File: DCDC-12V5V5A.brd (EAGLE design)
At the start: 40 x 23 mm, 34 parts, among them CN2 2828XX-2282834-2, CN3 2828XX-2282834-2, Q10 NMOSFET, Q9 NMOSFET, U1 LM3150MHX/NOPB

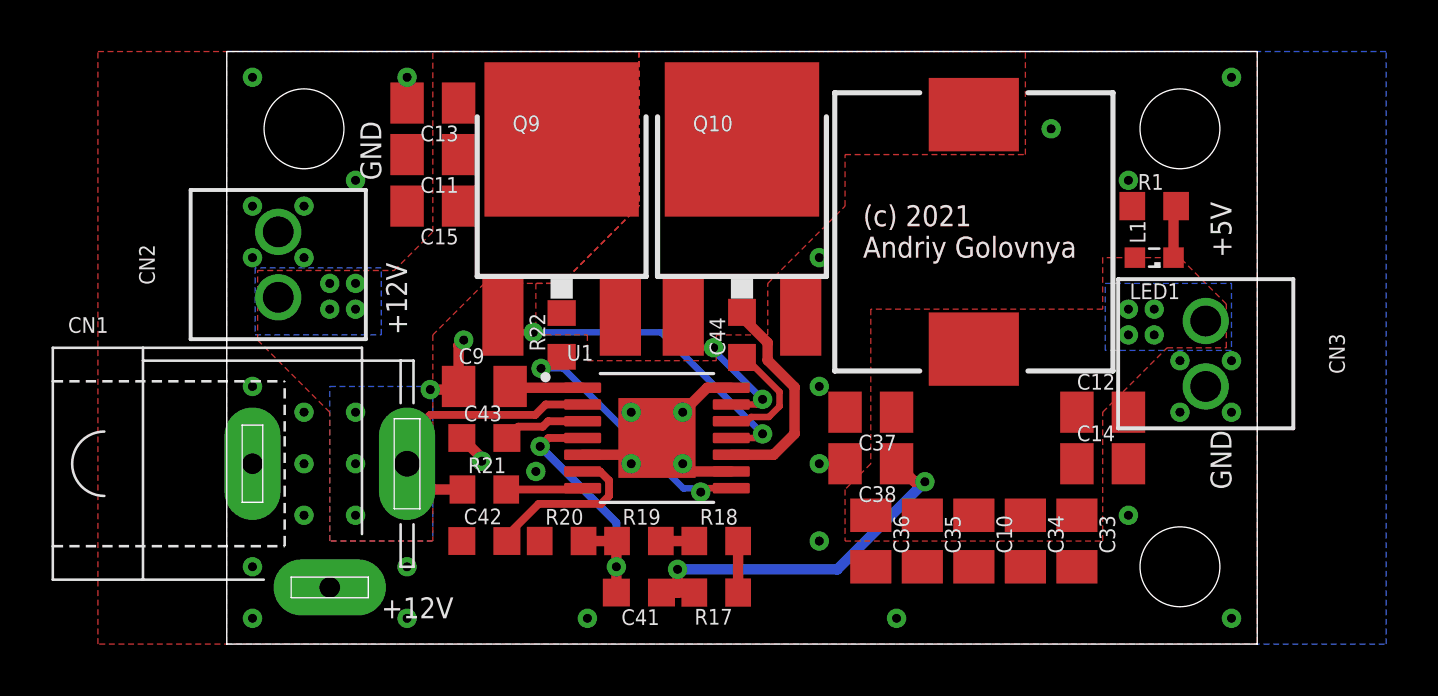
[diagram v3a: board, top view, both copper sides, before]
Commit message: Minor improvements in board routing. Generated CAM files. Fixed footprints in BoM.
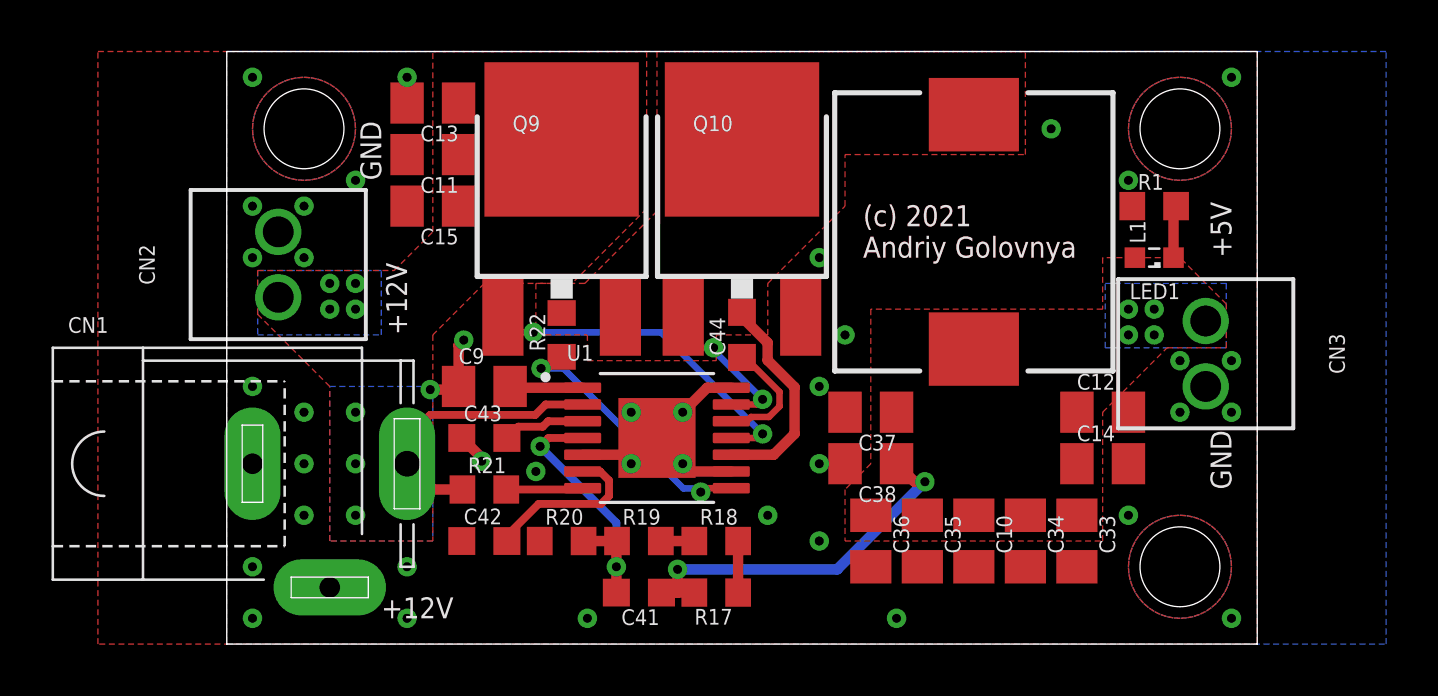
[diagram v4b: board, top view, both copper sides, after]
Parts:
- moved LOGO2 1.00 mm to (23.0, 1.00)
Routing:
- net GND: vias 38 -> 40
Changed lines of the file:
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@@
 <text x="4.1" y="14.5" size="0.8128" layer="22" font="vector" rot="MR270">+12V</text>
 <text x="4.1" y="17.1" size="0.8128" layer="22" font="vector" rot="MR270">GND</text>
-<text x="36.7" y="10.9" size="0.8128" layer="22" font="vector" rot="MR270">+5V</text>
-<text x="36.7" y="13.7" size="0.8128" layer="22" font="vector" rot="MR270">GND</text>
+<text x="36.7" y="13.5" size="0.8128" layer="22" font="vector" rot="MR270">+5V</text>
+<text x="36.7" y="11" size="0.8128" layer="22" font="vector" rot="MR270">GND</text>
 <text x="33" y="13" size="0.8128" layer="22" font="vector" rot="MR0">http://redscorp.net</text>
 <text x="24.7" y="15" size="0.8128" layer="1" font="vector" ratio="12">(c) 2021
@@
 </element>
 <element name="LOGO1" library="_my_logos" package="RSNURL_QR_8MM" value="RSNURL_QR_8MM" x="33" y="3" smashed="yes" rot="MR0"/>
-<element name="LOGO2" library="_my_logos" package="MFDEC_L_10MM" value="MFDECLOGO_L_10MM" x="24" y="1" smashed="yes" rot="MR0"/>
+<element name="LOGO2" library="_my_logos" package="MFDEC_L_10MM" value="MFDECLOGO_L_10MM" x="23" y="1" smashed="yes" rot="MR0"/>
 <element name="LED1" library="led" library_urn="urn:adsk.eagle:library:259" package="SML0603" package3d_urn="urn:adsk.eagle:package:15832/1" value="GREEN" x="36" y="15" smashed="yes" rot="R180">
 <attribute name="NAME" x="37" y="14" size="0.6096" layer="25" font="vector" rot="R180"/>
@@
 <vertex x="8" y="16"/>
 <vertex x="8" y="23"/>
-<vertex x="16" y="23"/>
-<vertex x="16" y="17"/>
-<vertex x="13" y="14"/>
+<vertex x="16.3" y="23"/>
+<vertex x="16.3" y="16.9"/>
+<vertex x="13.4" y="14"/>
 <vertex x="10" y="14"/>
 <vertex x="8" y="12"/>
 <vertex x="8" y="4"/>
 <vertex x="4" y="4"/>
-<vertex x="4" y="9"/>
-<vertex x="1.2" y="11.8"/>
-</polygon>
-<polygon width="0.1524" layer="16" thermals="no">
-<vertex x="1.1" y="14.6"/>
-<vertex x="1.1" y="12"/>
+<vertex x="4" y="10"/>
+<vertex x="1.2" y="12.8"/>
+</polygon>
+<polygon width="0.254" layer="16" thermals="no">
+<vertex x="1.2" y="14.5"/>
+<vertex x="1.2" y="12"/>
 <vertex x="6" y="12"/>
-<vertex x="6" y="14.6"/>
-</polygon>
-<polygon width="0.1524" layer="16" thermals="no">
+<vertex x="6" y="14.5"/>
+</polygon>
+<polygon width="0.254" layer="16" thermals="no">
 <vertex x="8" y="4"/>
 <vertex x="4" y="4"/>
@@
 <via x="1" y="10" extent="1-16" drill="0.35"/>
 <contactref element="R1" pad="1"/>
+<via x="24" y="12" extent="1-16" drill="0.35"/>
+<via x="21" y="5" extent="1-16" drill="0.35"/>
+<polygon width="0.1524" layer="1" pour="cutout">
+<vertex x="37" y="1" curve="-180"/>
+<vertex x="37" y="5" curve="-180"/>
+</polygon>
+<polygon width="0.1524" layer="1" pour="cutout">
+<vertex x="37" y="18" curve="-180"/>
+<vertex x="37" y="22" curve="-180"/>
+</polygon>
+<polygon width="0.1524" layer="1" pour="cutout">
+<vertex x="3" y="18" curve="-180"/>
+<vertex x="3" y="22" curve="-180"/>
+</polygon>
+<polygon width="0.1524" layer="16" pour="cutout">
+<vertex x="3" y="18" curve="-180"/>
+<vertex x="3" y="22" curve="-180"/>
+</polygon>
+<polygon width="0.1524" layer="16" pour="cutout">
+<vertex x="37" y="18" curve="-180"/>
+<vertex x="37" y="22" curve="-180"/>
+</polygon>
+<polygon width="0.1524" layer="16" pour="cutout">
+<vertex x="37" y="1" curve="-180"/>
+<vertex x="37" y="5" curve="-180"/>
+</polygon>
 </signal>
 <signal name="5V">
@@
 <vertex x="34" y="13"/>
 </polygon>
-<polygon width="0.1524" layer="16" thermals="no">
-<vertex x="39" y="11.4"/>
-<vertex x="34.1" y="11.4"/>
+<polygon width="0.254" layer="16" thermals="no">
+<vertex x="38.8" y="11.5"/>
+<vertex x="34.1" y="11.5"/>
 <vertex x="34.1" y="14"/>
-<vertex x="39" y="14"/>
+<vertex x="38.8" y="14"/>
 </polygon>
 <via x="35" y="13" extent="1-16" drill="0.35"/>
@@
 <vertex x="31" y="19"/>
 <vertex x="31" y="23"/>
-<vertex x="16" y="23"/>
-<vertex x="16" y="17"/>
-<vertex x="13" y="14"/>
+<vertex x="16.7" y="23"/>
+<vertex x="16.7" y="16.8"/>
+<vertex x="13.9" y="14"/>
 <vertex x="12" y="14"/>
 <vertex x="12" y="12"/>

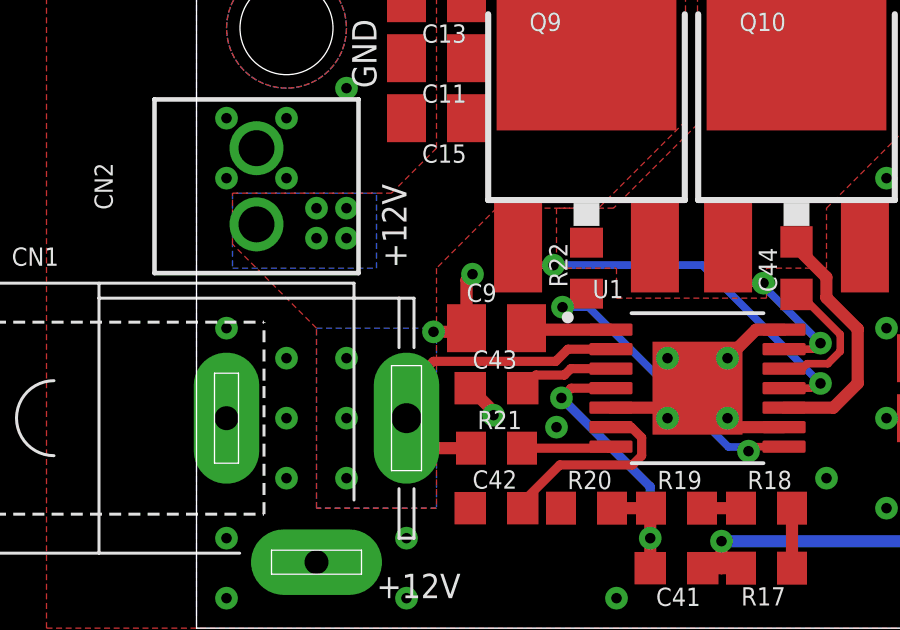
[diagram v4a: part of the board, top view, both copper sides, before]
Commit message: Minor improvements in board routing. Generated CAM files.
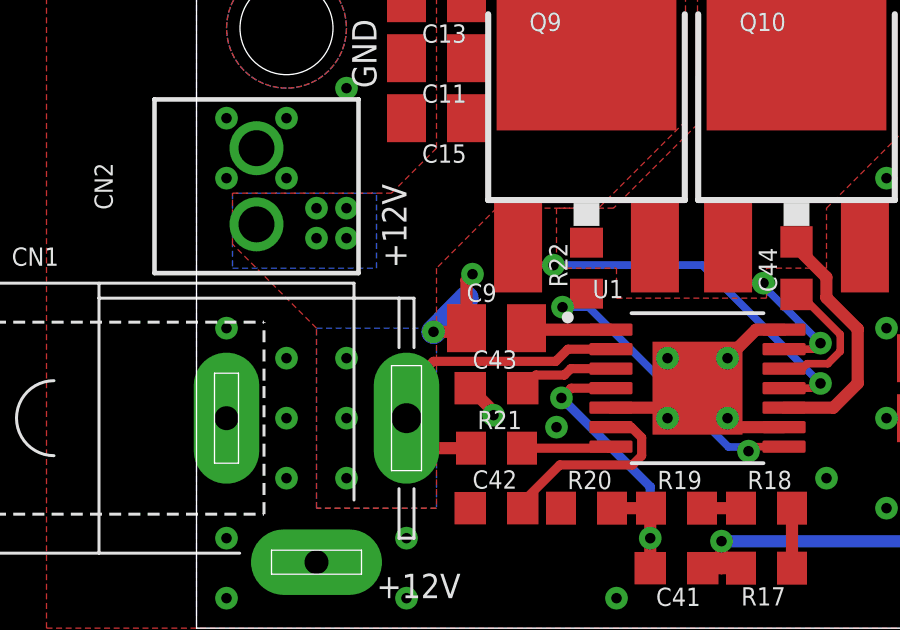
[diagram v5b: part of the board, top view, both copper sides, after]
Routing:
- net GND: track 10.6 -> 12.1 mm
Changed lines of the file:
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@@
 <vertex x="37" y="5" curve="-180"/>
 </polygon>
+<wire x1="7.9" y1="9.8782" x2="9" y2="11" width="0.8128" layer="16"/>
 </signal>
 <signal name="5V">

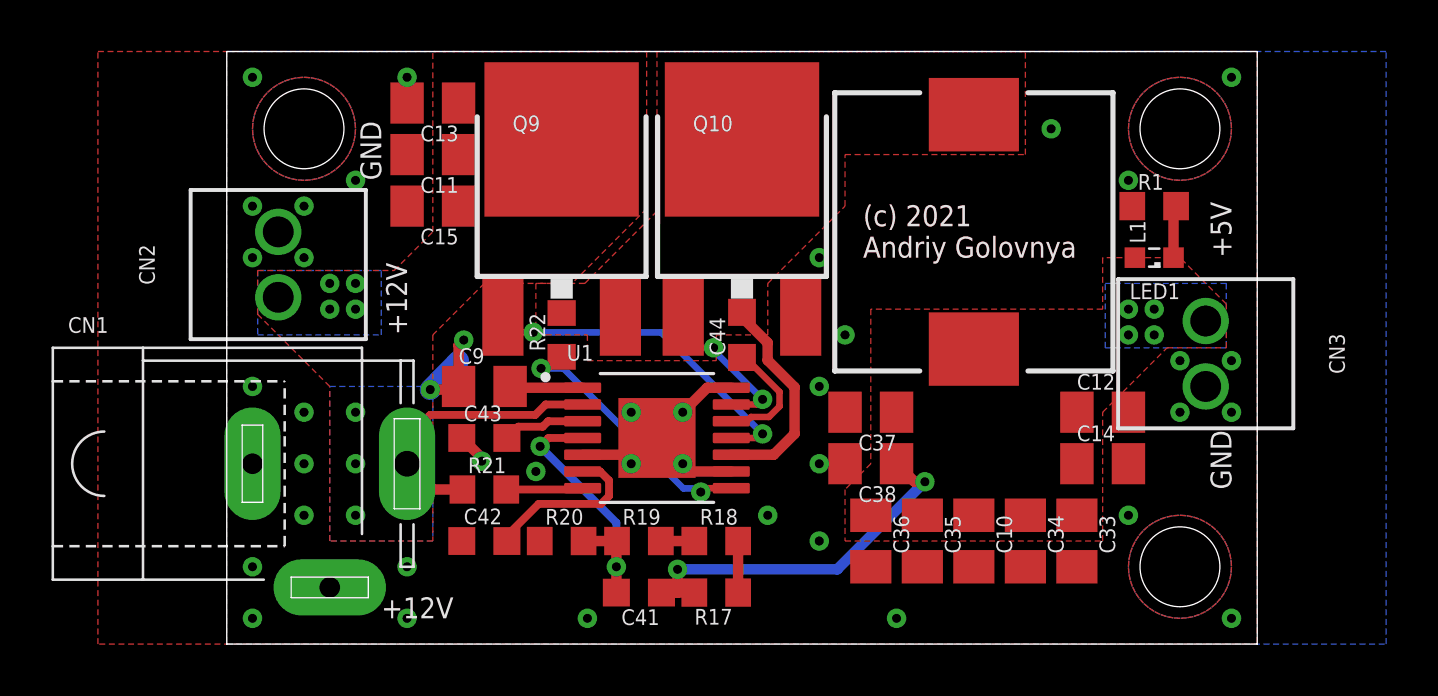
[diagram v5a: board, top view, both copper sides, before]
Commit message: Added tooling holes. Generated CAM files.
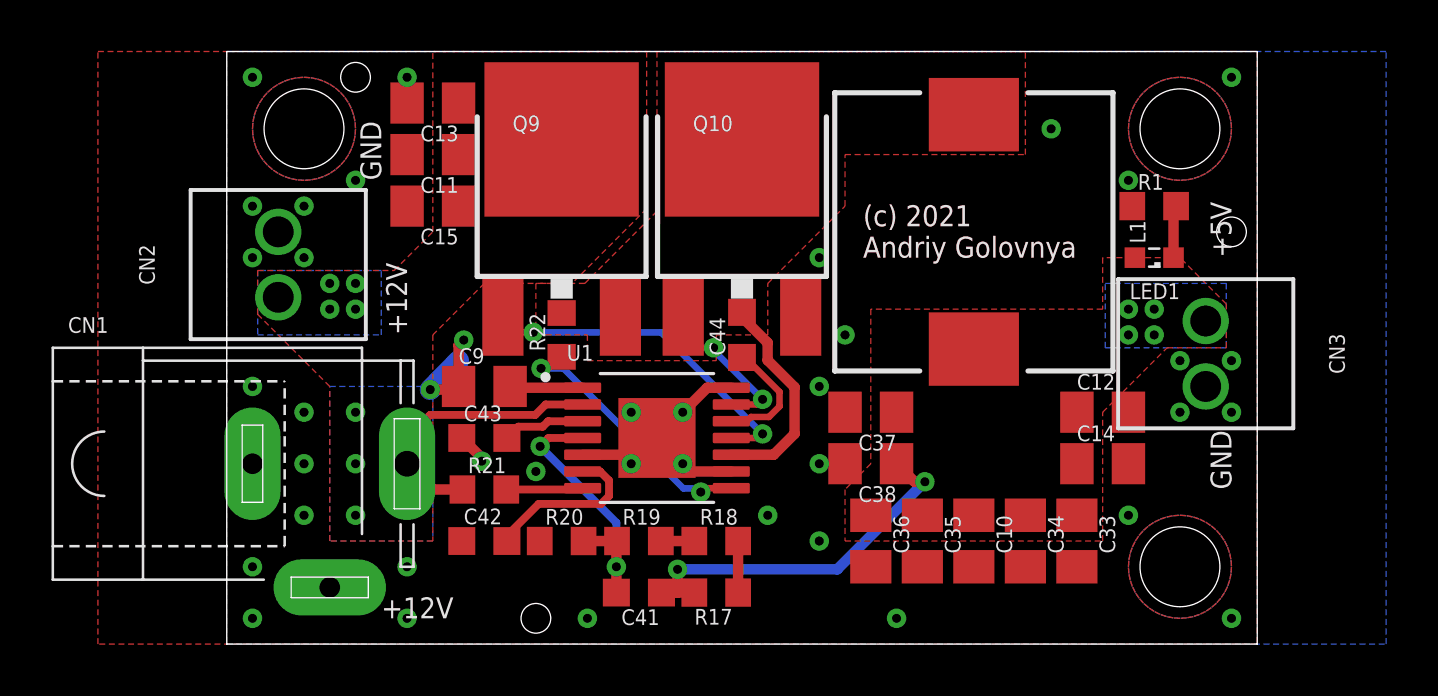
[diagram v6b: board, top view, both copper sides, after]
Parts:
- added HOLE1, HOLE2, HOLE3: TOOLINGHOLE, _my_fiducia:TOOLING-HOLE
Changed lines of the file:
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@@
 <layer number="136" name="silktop" color="7" fill="1" visible="yes" active="yes"/>
 <layer number="137" name="silkbottom" color="7" fill="1" visible="yes" active="yes"/>
+<layer number="138" name="EEE" color="7" fill="1" visible="yes" active="yes"/>
+<layer number="139" name="_tKeepout" color="7" fill="1" visible="yes" active="yes"/>
+<layer number="141" name="ASSEMBLY_TOP" color="7" fill="1" visible="yes" active="yes"/>
+<layer number="143" name="PLACE_BOUND_TOP" color="7" fill="1" visible="yes" active="yes"/>
 <layer number="144" name="Drill_legend" color="7" fill="1" visible="yes" active="yes"/>
 <layer number="145" name="DrillLegend_01-16" color="7" fill="1" visible="yes" active="yes"/>
 <layer number="146" name="DrillLegend_01-20" color="7" fill="1" visible="yes" active="yes"/>
+<layer number="147" name="PIN_NUMBER" color="7" fill="1" visible="yes" active="yes"/>
 <layer number="150" name="Notes" color="7" fill="1" visible="yes" active="yes"/>
 <layer number="151" name="HeatSink" color="7" fill="1" visible="yes" active="yes"/>
@@
 <layer number="154" name="FabDoc2" color="7" fill="1" visible="yes" active="yes"/>
 <layer number="155" name="FabDoc3" color="7" fill="1" visible="yes" active="yes"/>
+<layer number="166" name="AntennaArea" color="7" fill="1" visible="yes" active="yes"/>
+<layer number="168" name="4mmHeightArea" color="7" fill="1" visible="yes" active="yes"/>
 <layer number="199" name="Contour" color="7" fill="1" visible="yes" active="yes"/>
 <layer number="200" name="200bmp" color="1" fill="10" visible="yes" active="yes"/>
@@
 <attribute name="VALUE" x="35.365" y="15.095" size="0.6096" layer="27" font="vector"/>
 </element>
+<element name="HOLE1" library="_my_fiducia" package="TOOLING-HOLE" value="TOOLINGHOLE" x="39" y="16" smashed="yes"/>
+<element name="HOLE2" library="_my_fiducia" package="TOOLING-HOLE" value="TOOLINGHOLE" x="5" y="22" smashed="yes"/>
+<element name="HOLE3" library="_my_fiducia" package="TOOLING-HOLE" value="TOOLINGHOLE" x="12" y="1" smashed="yes"/>
 </elements>
 <signals>

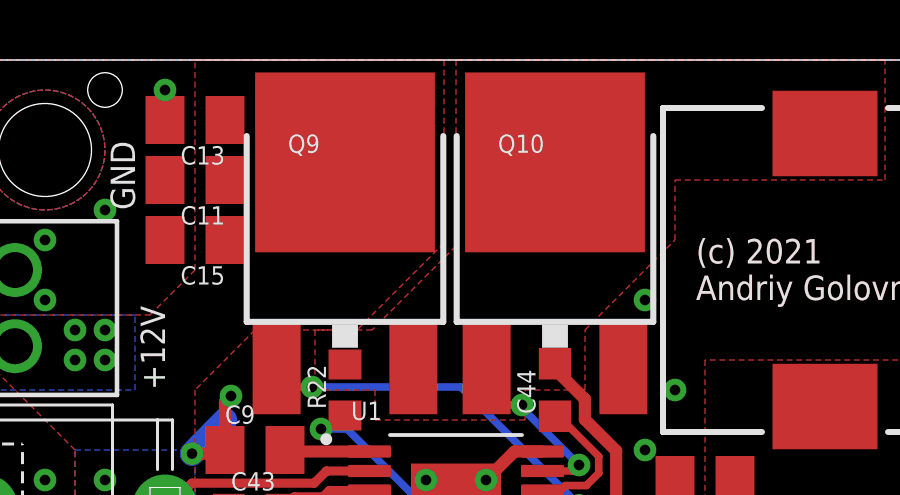
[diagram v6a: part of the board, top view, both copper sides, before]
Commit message: Added copper thermal pads at the back of the board.
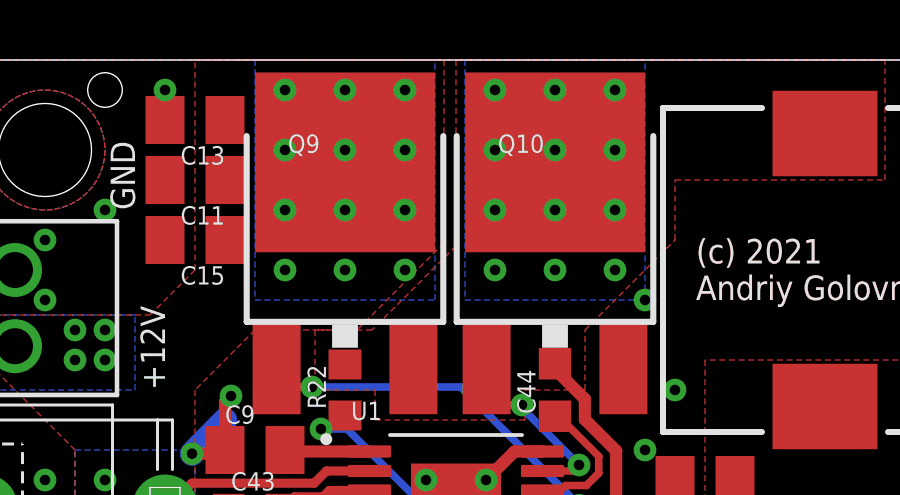
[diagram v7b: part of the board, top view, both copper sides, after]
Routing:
- net BUCK_SW: vias 0 -> 12
- net 12V: vias 7 -> 19
- added copper zone on layer 16, net BUCK_SW
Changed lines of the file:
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@@
 <layer number="29" name="tStop" color="7" fill="3" visible="yes" active="yes"/>
 <layer number="30" name="bStop" color="7" fill="6" visible="yes" active="yes"/>
-<layer number="31" name="tCream" color="7" fill="4" visible="no" active="yes"/>
-<layer number="32" name="bCream" color="7" fill="5" visible="no" active="yes"/>
+<layer number="31" name="tCream" color="7" fill="4" visible="yes" active="yes"/>
+<layer number="32" name="bCream" color="7" fill="5" visible="yes" active="yes"/>
 <layer number="33" name="tFinish" color="6" fill="3" visible="no" active="yes"/>
 <layer number="34" name="bFinish" color="6" fill="6" visible="no" active="yes"/>
@@
 </elements>
 <signals>
-<signal name="12V">
+<signal name="12V" airwireshidden="yes">
 <contactref element="Q9" pad="4"/>
 <contactref element="U1" pad="2"/>
@@
 <via x="5" y="7" extent="1-16" drill="0.35"/>
 <via x="5" y="5" extent="1-16" drill="0.35"/>
+<polygon width="0.254" layer="16" thermals="no">
+<vertex x="10" y="23"/>
+<vertex x="10" y="15"/>
+<vertex x="16" y="15"/>
+<vertex x="16" y="23"/>
+</polygon>
+<via x="11" y="22" extent="1-16" drill="0.35"/>
+<via x="15" y="22" extent="1-16" drill="0.35"/>
+<via x="13" y="22" extent="1-16" drill="0.35"/>
+<via x="11" y="20" extent="1-16" drill="0.35"/>
+<via x="13" y="20" extent="1-16" drill="0.35"/>
+<via x="15" y="20" extent="1-16" drill="0.35"/>
+<via x="15" y="18" extent="1-16" drill="0.35"/>
+<via x="13" y="18" extent="1-16" drill="0.35"/>
+<via x="11" y="18" extent="1-16" drill="0.35"/>
+<via x="11" y="16" extent="1-16" drill="0.35"/>
+<via x="13" y="16" extent="1-16" drill="0.35"/>
+<via x="15" y="16" extent="1-16" drill="0.35"/>
 </signal>
 <signal name="GND" airwireshidden="yes">
@@
 <wire x1="11.31" y1="12.1" x2="10.72" y2="12.69" width="0.254" layer="1"/>
 </signal>
-<signal name="BUCK_SW">
+<signal name="BUCK_SW" airwireshidden="yes">
 <contactref element="U1" pad="10"/>
 <contactref element="R22" pad="2"/>
@@
 <vertex x="14" y="12"/>
 </polygon>
+<polygon width="0.254" layer="16" thermals="no">
+<vertex x="17" y="23"/>
+<vertex x="17" y="15"/>
+<vertex x="23" y="15"/>
+<vertex x="23" y="23"/>
+</polygon>
+<via x="18" y="22" extent="1-16" drill="0.35"/>
+<via x="20" y="22" extent="1-16" drill="0.35"/>
+<via x="22" y="22" extent="1-16" drill="0.35"/>
+<via x="22" y="20" extent="1-16" drill="0.35"/>
+<via x="20" y="20" extent="1-16" drill="0.35"/>
+<via x="18" y="20" extent="1-16" drill="0.35"/>
+<via x="18" y="18" extent="1-16" drill="0.35"/>
+<via x="20" y="18" extent="1-16" drill="0.35"/>
+<via x="22" y="18" extent="1-16" drill="0.35"/>
+<via x="22" y="16" extent="1-16" drill="0.35"/>
+<via x="20" y="16" extent="1-16" drill="0.35"/>
+<via x="18" y="16" extent="1-16" drill="0.35"/>
 </signal>
 <signal name="N$9">
